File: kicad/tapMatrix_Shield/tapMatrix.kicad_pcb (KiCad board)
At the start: 2 copper layers, 68.6 x 53.3 mm, 29 parts, among them P5 TS_ZIF, P6 LED_MATRIX_HDR, U1 MCP1700T-3302E/MB, U2 MCP4921-E/SN, U3 74LS125, U4 TL072, U5 SD_CARD, U6 DS1307

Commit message: revised C3 to link to tapMatrix library, other minor edits
re-routed C3
repositioned reference labels for caps
changed U1 line width to be consistent with other components
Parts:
- C3: footprint Capacitors_SMD:c_0603 -> tapmatrix:C_0603
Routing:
- net GND: vias 15 -> 16

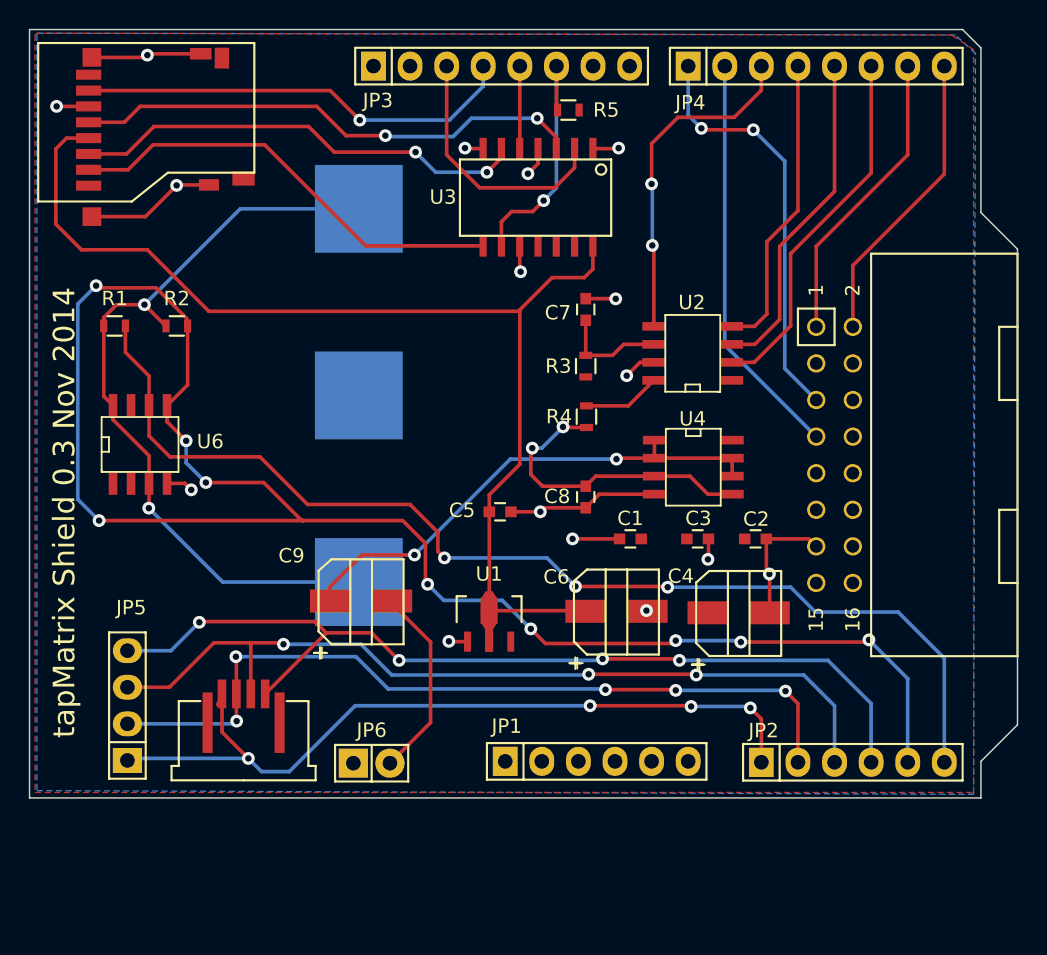
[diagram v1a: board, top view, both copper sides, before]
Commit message: corrected uSD connector footprint
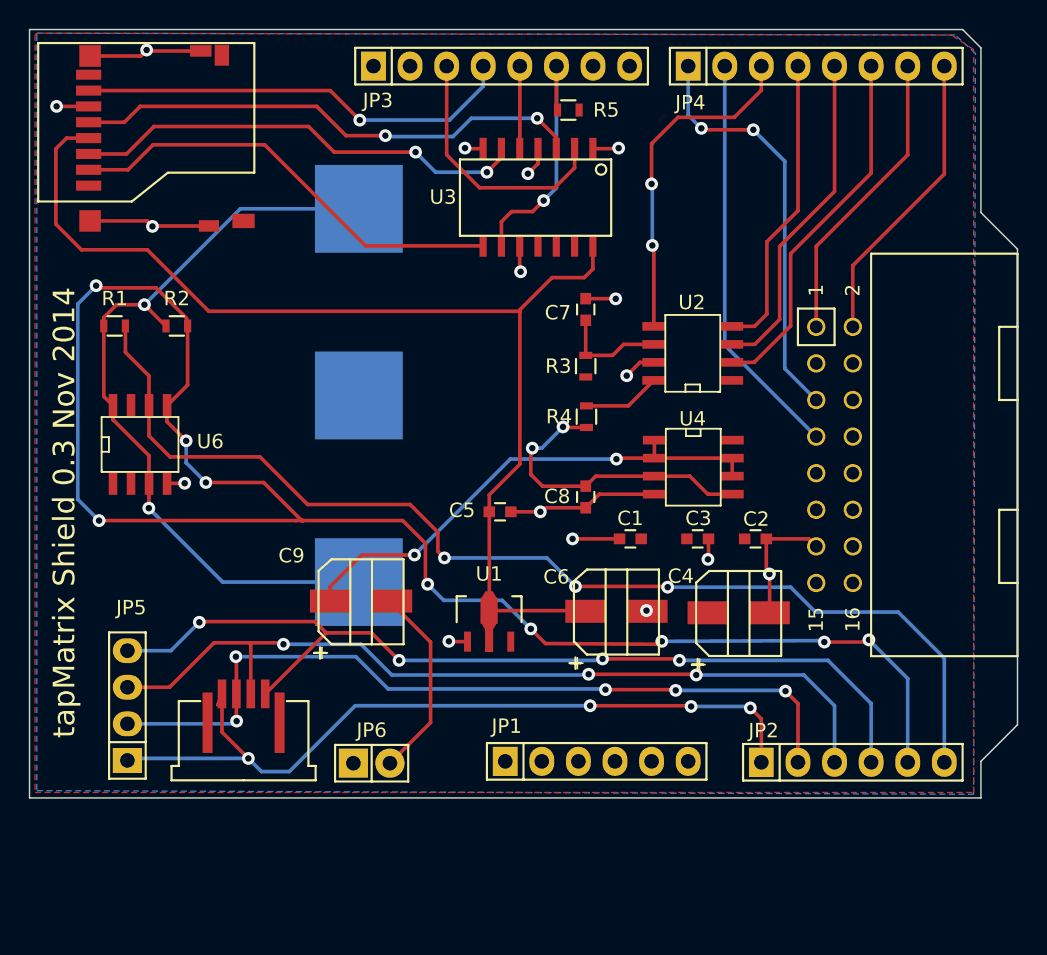
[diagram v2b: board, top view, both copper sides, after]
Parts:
- U5: footprint tapmatrix:114-00841-68 -> 114-00841-68
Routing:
- net GND: track 57.5 -> 56.5 mm

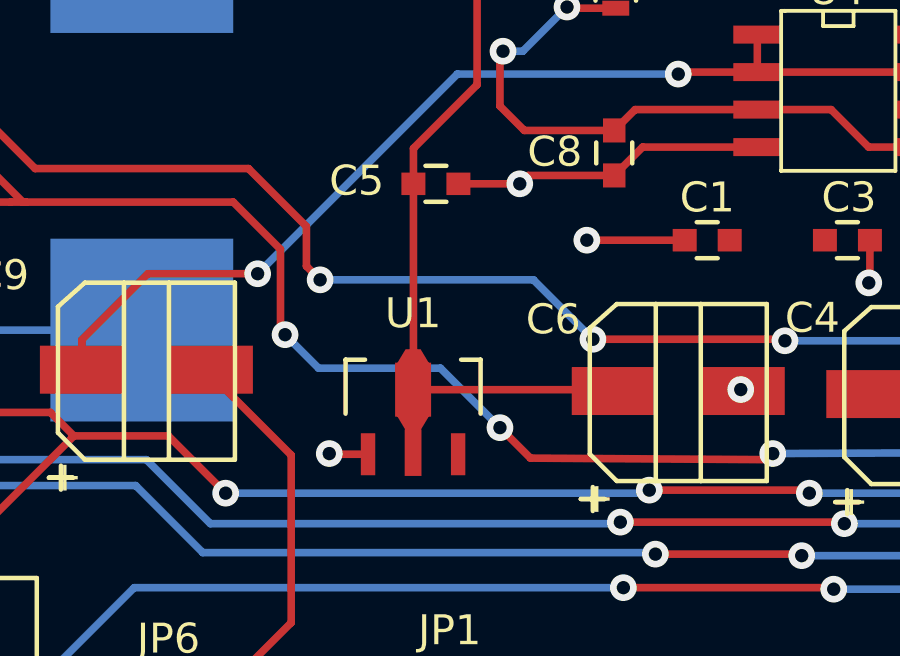
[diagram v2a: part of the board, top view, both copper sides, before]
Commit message: corrected error with U1 pins (2 and 3 were reversed)
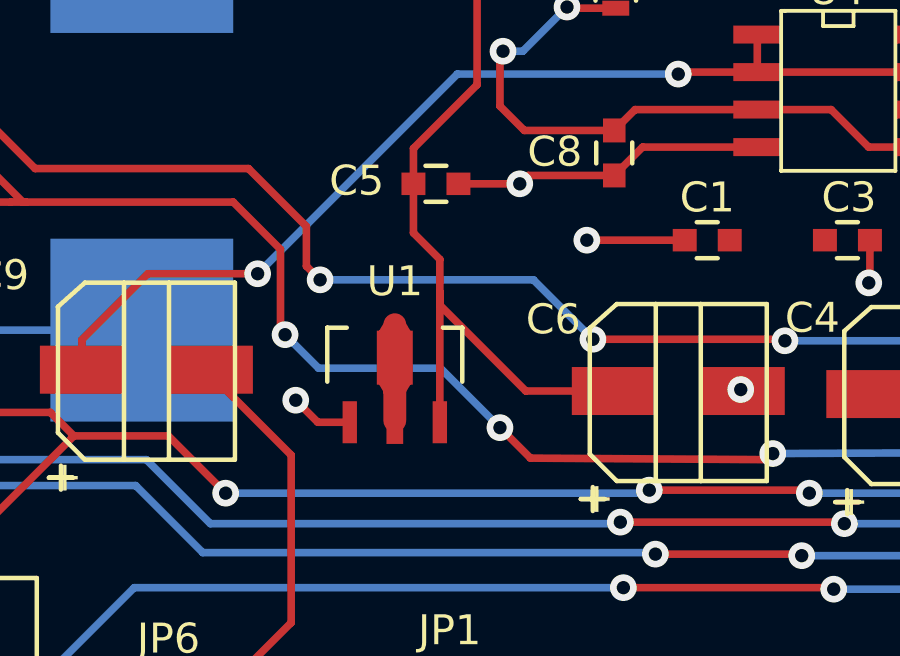
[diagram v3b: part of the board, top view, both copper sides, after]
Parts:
- moved U1 1.23 mm to (162.1, 125.9)
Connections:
- U1 pad 2: +3.3V -> +5V
- U1 pad 3: +5V -> +3.3V
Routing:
- net +5V: track 0.06 -> 4.36 mm
- net +3.3V: track 82.0 -> 81.1 mm
- net GND: track 56.5 -> 57.3 mm

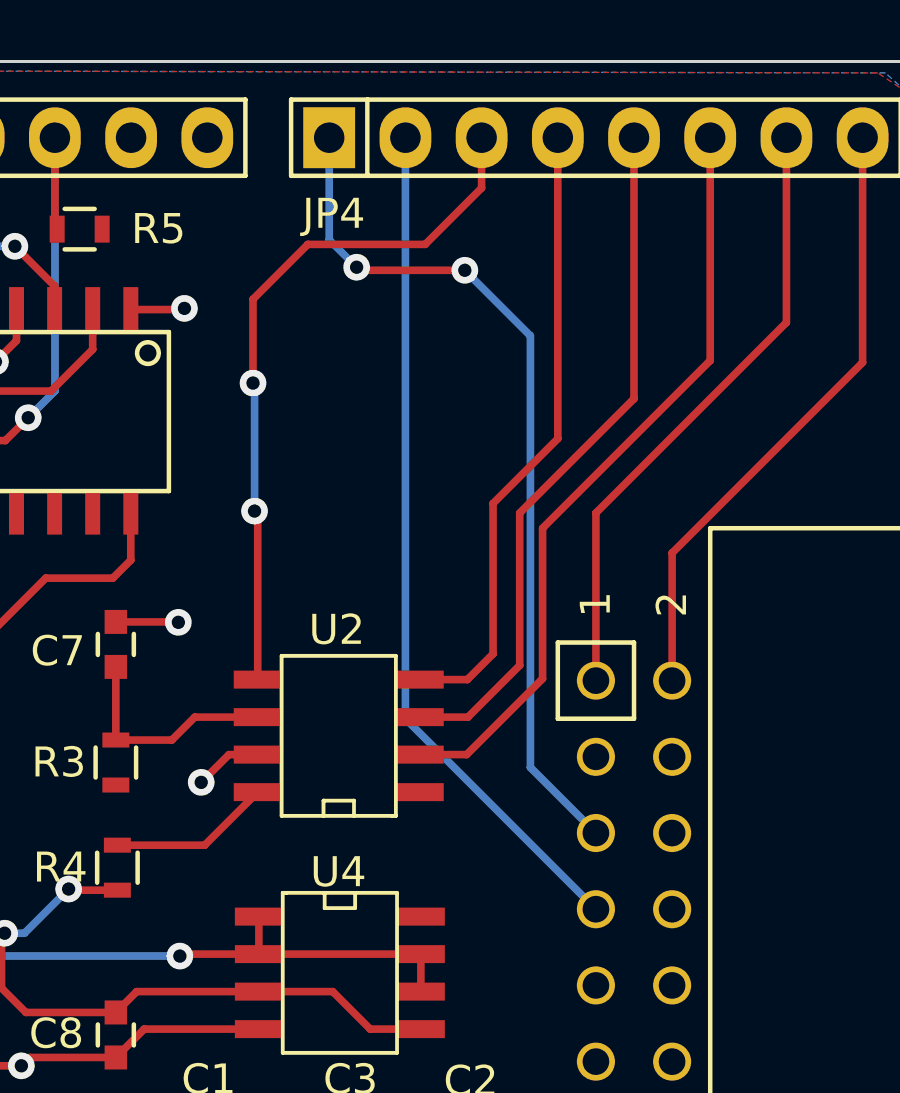
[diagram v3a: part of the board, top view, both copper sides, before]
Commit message: corrected JP4, where MATRIX_WR and MATRIX_DATA were reveresed
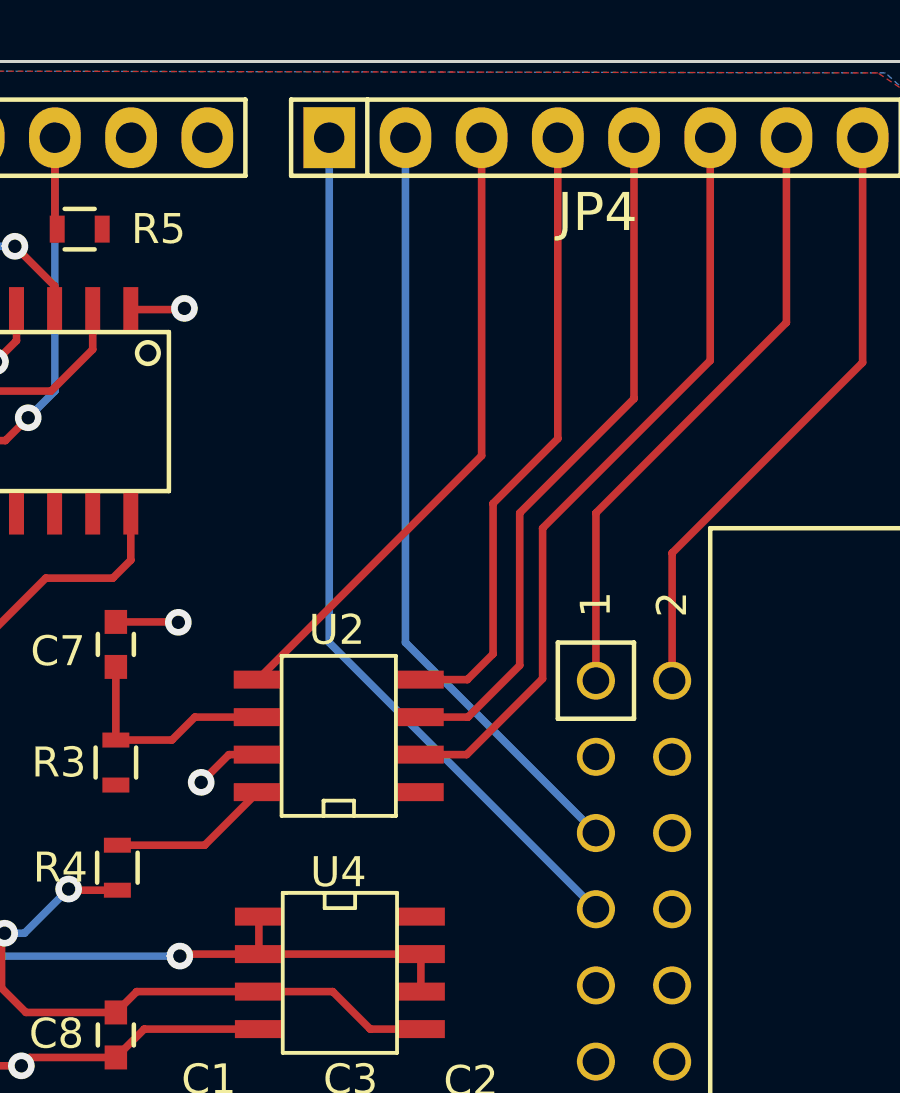
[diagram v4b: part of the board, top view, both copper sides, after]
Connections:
- JP4 pad 1: /MATRIX_WR -> /MATRIX_DATA
- JP4 pad 2: /MATRIX_DATA -> /MATRIX_WR
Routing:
- net /MATRIX_WR: track 28.9 -> 25.8 mm, vias 2 -> 0
- net /DAC_LAT: track 24.8 -> 22.4 mm, vias 2 -> 0
- net /MATRIX_DATA: track 28.3 -> 29.4 mm

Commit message: add footprints and headers, tear up layout
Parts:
- added JP7: 6_PIN_3, tapmatrix:Pin_Header_Straight_1x06, F.Cu at (142.2, 137.2)
- added RV1: POT, tapmatrix:TC33X, F.Cu at (152.4, 143.5)
- U4: value TL072 -> TS922; footprint tapmatrix:SOIC-8_N -> tapmatrix:TS922_SO8
- U6: value DS1307 -> DS3231; footprint tapmatrix:SOIC-8_N -> tapmatrix:DS3231
- moved JP5 47.8 mm to (185.4, 134.6), turned to 0 degrees
- moved P5 13.2 mm to (137.2, 143.5)
- moved JP6 2.92 mm to (157.5, 137.2)
- moved U6 2.13 mm to (138.4, 113.0), turned to 180 degrees
- moved U4 1.22 mm to (176.5, 115.6)
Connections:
- R1 pad 1: Net-(BT1-Pad1) -> +5V
- R2 pad 1: Net-(BT1-Pad1) -> +5V
- U1 pad 2: +5V -> +3.3V
- U1 pad 3: +3.3V -> +5V
- U4 pad 3: Net-(C8-Pad1) -> Net-(RV1-Pad2)
- U4 pad 5: Net-(C8-Pad1) -> Net-(RV1-Pad2)
- U6 pad 2: Net-(U6-Pad2) -> +5V
- U6 pad 3: Net-(BT1-Pad1) -> Net-(U6-Pad3)
- U6 pad 4: GND -> Net-(U6-Pad4)
- U6 pad 5: /I2C_SDA -> GND
- U6 pad 6: /I2C_SCL -> GND
- U6 pad 7: Net-(U6-Pad7) -> GND
- U6 pad 8: Net-(BT1-Pad1) -> GND
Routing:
- net /I2C_SDA: track 113.6 -> 0.00 mm, vias 9 -> 0
- net /I2C_SCL: track 77.9 -> 0.00 mm, vias 3 -> 0
- net /YM: track 65.0 -> 0.00 mm, vias 4 -> 0
- net /XP: track 59.7 -> 0.00 mm, vias 3 -> 0
- net /XM: track 56.7 -> 0.00 mm, vias 4 -> 0
- net /YP: track 56.6 -> 0.00 mm, vias 5 -> 0
- net Net-(BT1-Pad1): track 54.2 -> 0.00 mm, vias 2 -> 0
- net Net-(C9-Pad1): track 35.1 -> 0.00 mm, vias 2 -> 0
- net Net-(C8-Pad1): track 21.4 -> 0.00 mm, vias 2 -> 0
- net Net-(C9-Pad2): track 13.5 -> 0.00 mm
- net +3.3V: track 81.1 -> 74.2 mm
- net +5V: track 4.36 -> 11.2 mm
- net GND: track 57.3 -> 54.9 mm, vias 16 -> 15
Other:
- board text added: "tapMatrix Shield 0.4 Dec 2014"
- board text removed: "tapMatrix Shield 0.3 Nov 2014"

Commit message: Create Gerbers for 0.4
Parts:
- P5: value TS_ZIF -> P5
- moved RV1 29.0 mm to (160.0, 115.6), turned to 270 degrees
- moved R2 19.6 mm to (146.7, 125.7), turned to 90 degrees
- moved R1 19.6 mm to (142.2, 125.7), turned to 90 degrees
- moved P5 13.5 mm to (146.1, 133.3)
- moved JP7 8.13 mm to (137.2, 130.8), turned to 90 degrees
- moved U6 6.35 mm to (144.8, 113.0), turned to 90 degrees
- moved JP5 1.27 mm to (185.4, 133.3)
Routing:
- net /I2C_SDA: track 0.00 -> 96.3 mm, vias 0 -> 3
- net /I2C_SCL: track 0.00 -> 79.2 mm, vias 0 -> 6
- net /YM: track 0.00 -> 56.1 mm, vias 0 -> 2
- net Net-(BT1-Pad1): track 0.00 -> 53.6 mm, vias 0 -> 2
- net Net-(C9-Pad1): track 0.00 -> 51.3 mm, vias 0 -> 4
- net /XP: track 0.00 -> 51.0 mm, vias 0 -> 2
- net /YP: track 0.00 -> 46.0 mm, vias 0 -> 2
- net /XM: track 0.00 -> 40.3 mm, vias 0 -> 2
- net +3.3V: track 74.2 -> 114.4 mm, vias 0 -> 3
- net Net-(RV1-Pad2): track 0.00 -> 23.8 mm, vias 0 -> 2
- net GND: track 54.9 -> 76.8 mm, vias 15 -> 18
- net Net-(C8-Pad1): track 0.00 -> 17.6 mm, vias 0 -> 2
- net Net-(C9-Pad2): track 0.00 -> 16.7 mm, vias 0 -> 1
- net +5V: track 11.2 -> 0.06 mm
- net Net-(R4-Pad2): track 5.41 -> 8.05 mm, vias 0 -> 2
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
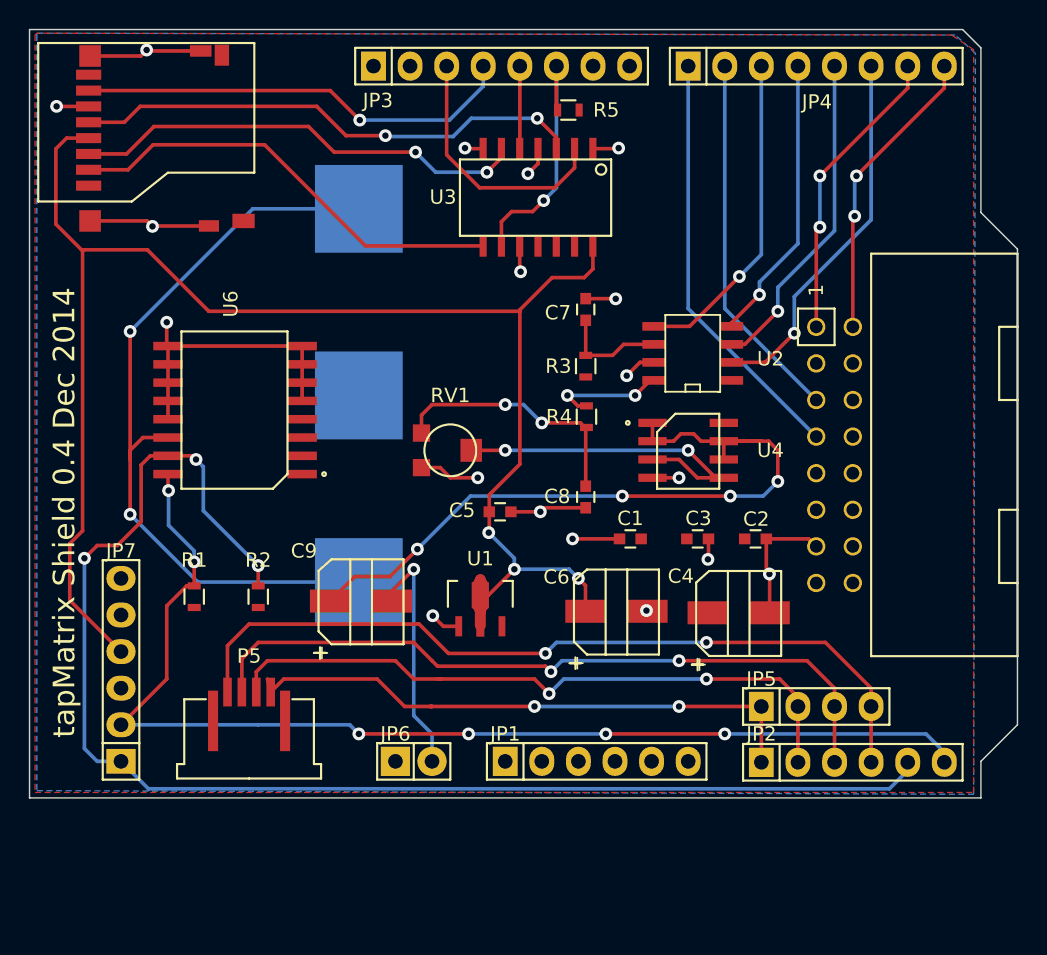
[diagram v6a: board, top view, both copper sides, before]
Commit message: Correct reversed pins 2+3 on LDO
Input and output pins were reversed on the MCP1703 voltage regulator.
Corrected schematic, footprint, and layout.
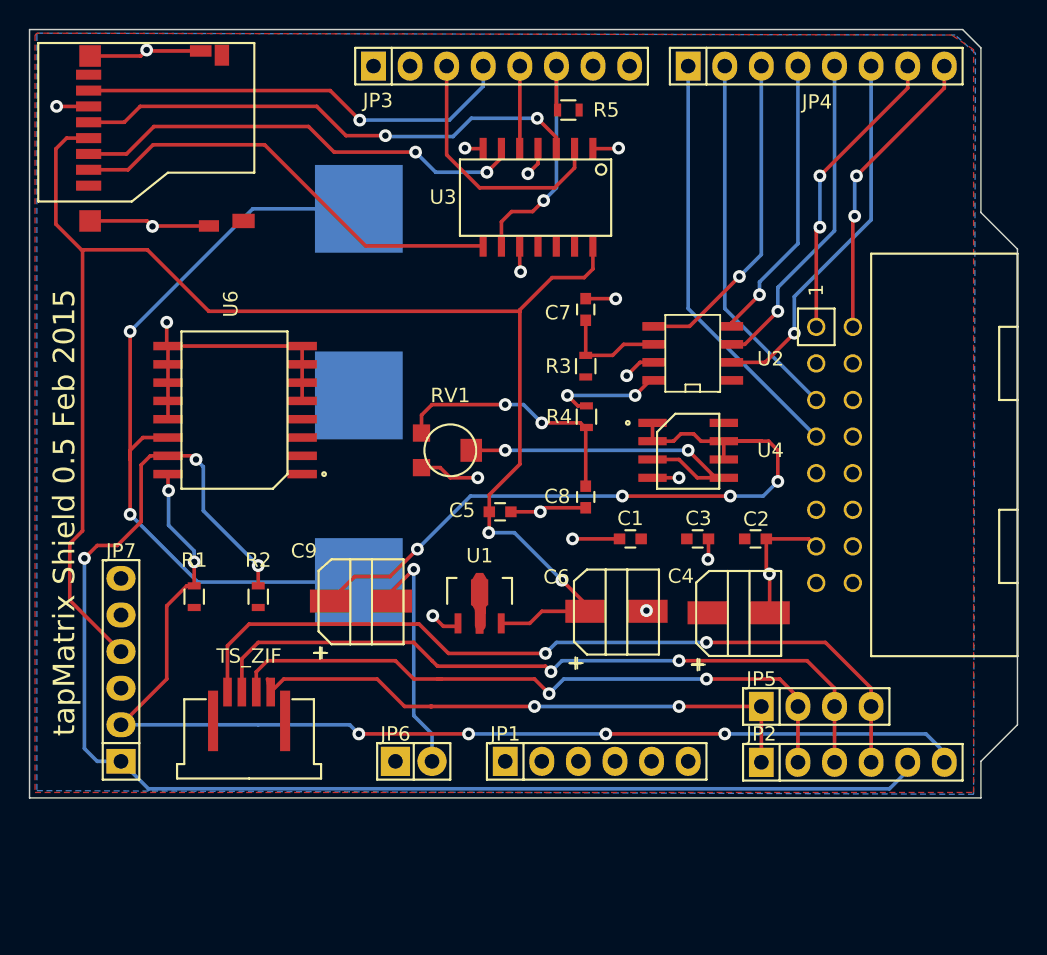
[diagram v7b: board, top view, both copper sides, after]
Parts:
- P5: value P5 -> TS_ZIF
- U1: value MCP1700T-3302E/MB -> MCP1703
- U2: footprint tapmatrix:SOIC-8_N -> SOIC-8_N
- moved U1 0.21 mm to (162.1, 125.7)
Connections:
- U1 pad 2: +3.3V -> +5V
- U1 pad 3: +5V -> +3.3V
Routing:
- net +5V: track 0.06 -> 4.36 mm
- net +3.3V: track 114.4 -> 112.0 mm, vias 3 -> 2
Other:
- board text added: "tapMatrix Shield 0.5 Feb 2015"
- board text removed: "tapMatrix Shield 0.4 Dec 2014"

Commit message: 0.4.1 revision - new level shifter component, etc
Replace quad buffer / level shifter with 74AHC125N components tolerant
of VCC=3.3V. Correct mixed pins on LDO. Add labels for breakout pins,
and refine silkscreen text.
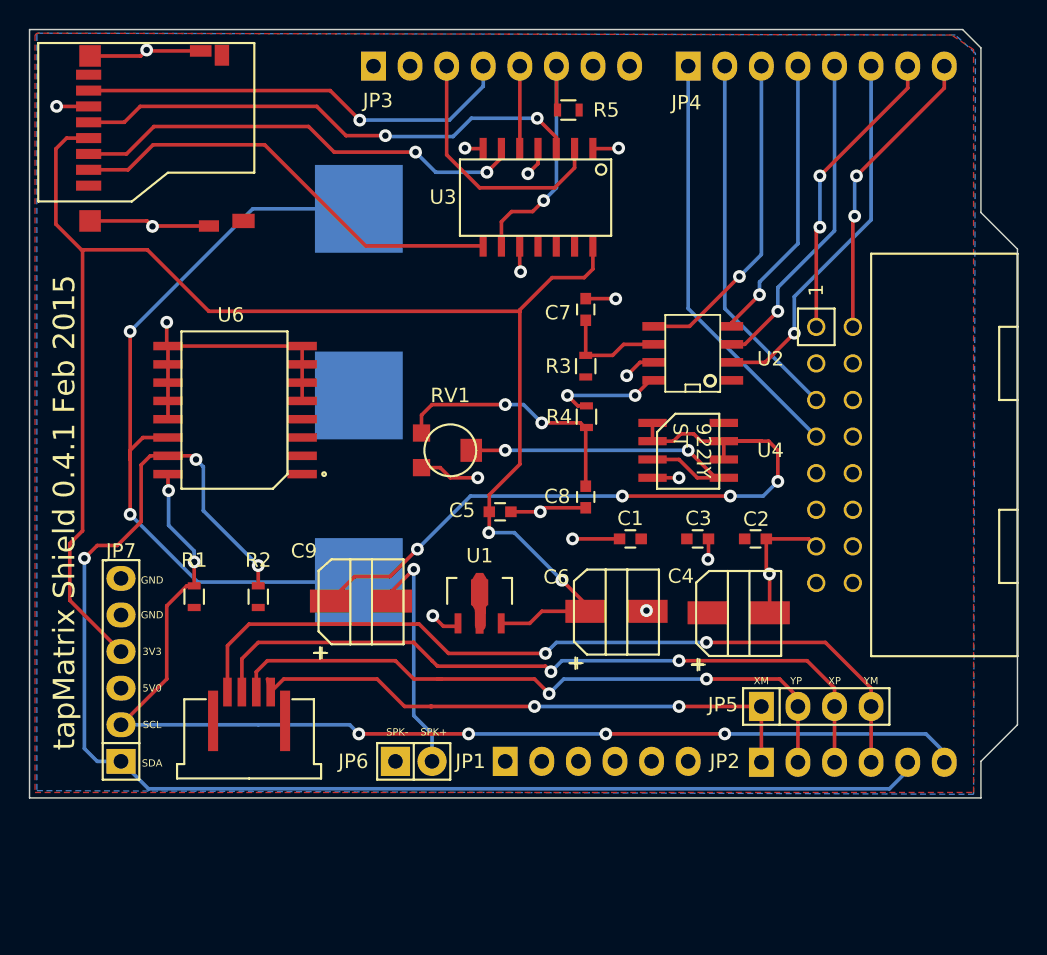
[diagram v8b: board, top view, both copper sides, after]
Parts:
- BT1: value BATTERY -> CR2032
- U4: footprint tapmatrix:TS922_SO8 -> TS922_SO8
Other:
- board text added: "(c) 2015 Responsive Devices Inc"
- board text added: "3V3"
- board text added: "5V0"
- board text added: "922IY ST"
- board text added: "SPK+"
- board text added: "SPK-"
- board text added: "XM"
- board text added: "XP"
- board text added: "YM"
- board text added: "YP"
- board text added: "tapMatrix Shield 0.4.1 Feb 2015"
- board text removed: "(c) 2014 Responsive Devices Inc"
- board text removed: "tapMatrix Shield 0.5 Feb 2015"
